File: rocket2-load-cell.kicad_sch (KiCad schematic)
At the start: 42 parts, among them J1 SWD, J2 629105150521, J3 PJ-002A, J4 Conn_01x02, U1 STM32F103C8Tx, U3 LD1117V33, Y1 16MHz

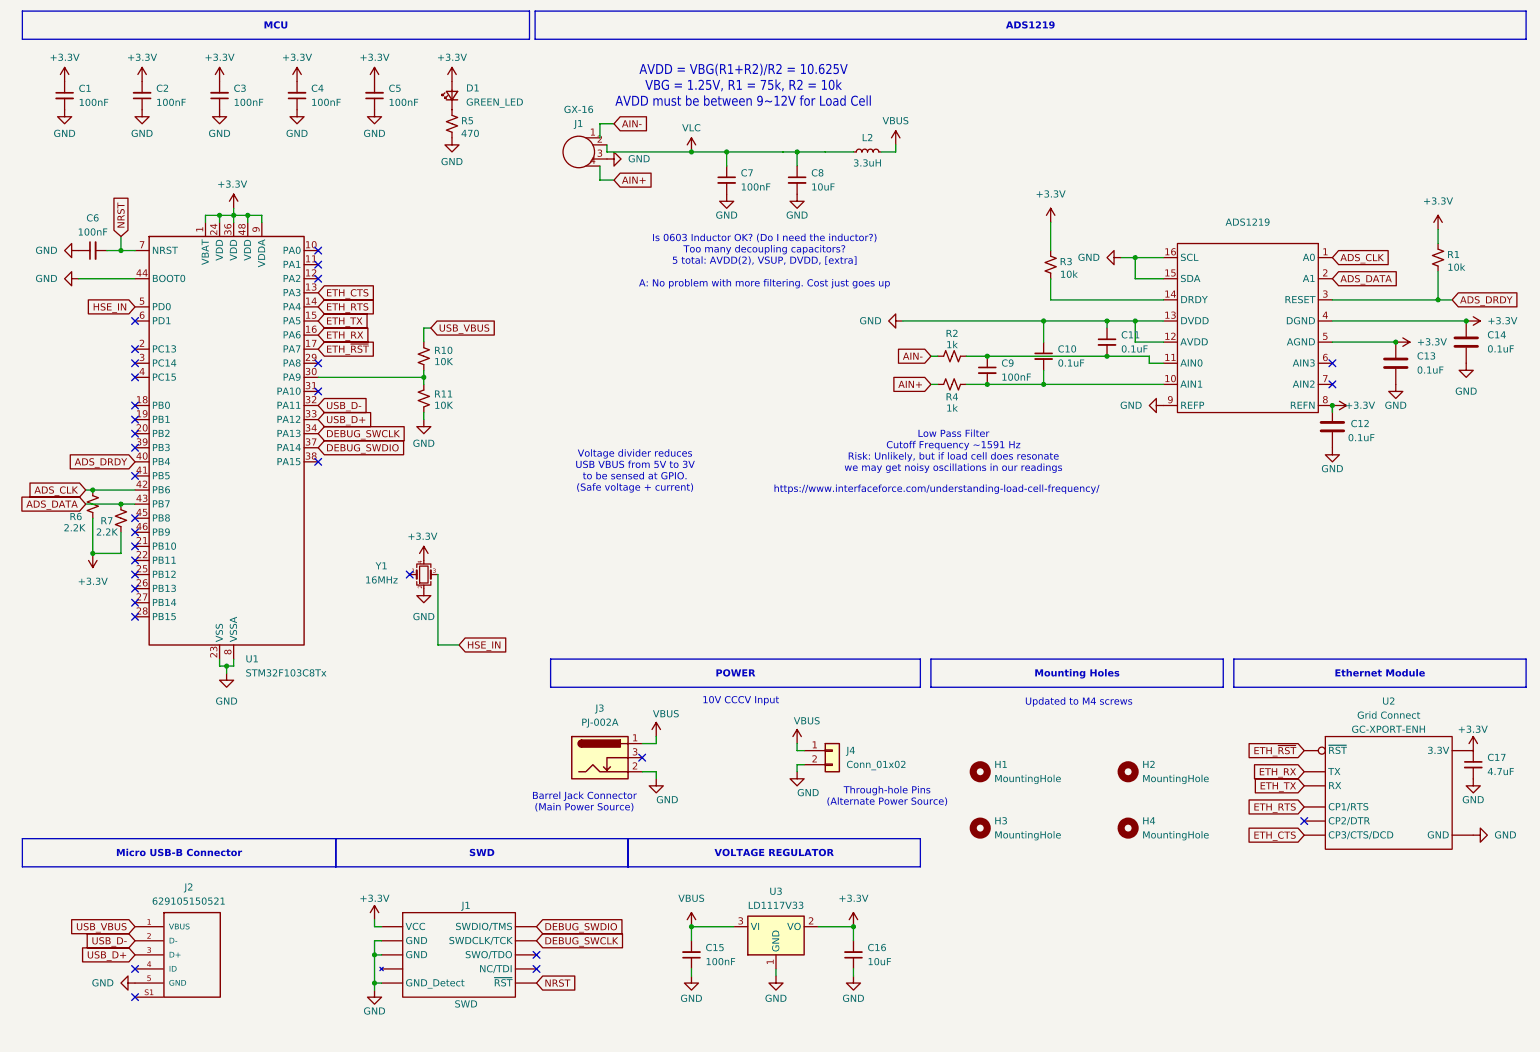
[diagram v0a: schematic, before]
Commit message: Layout adjustments
Layout revisions based on CDR feedback
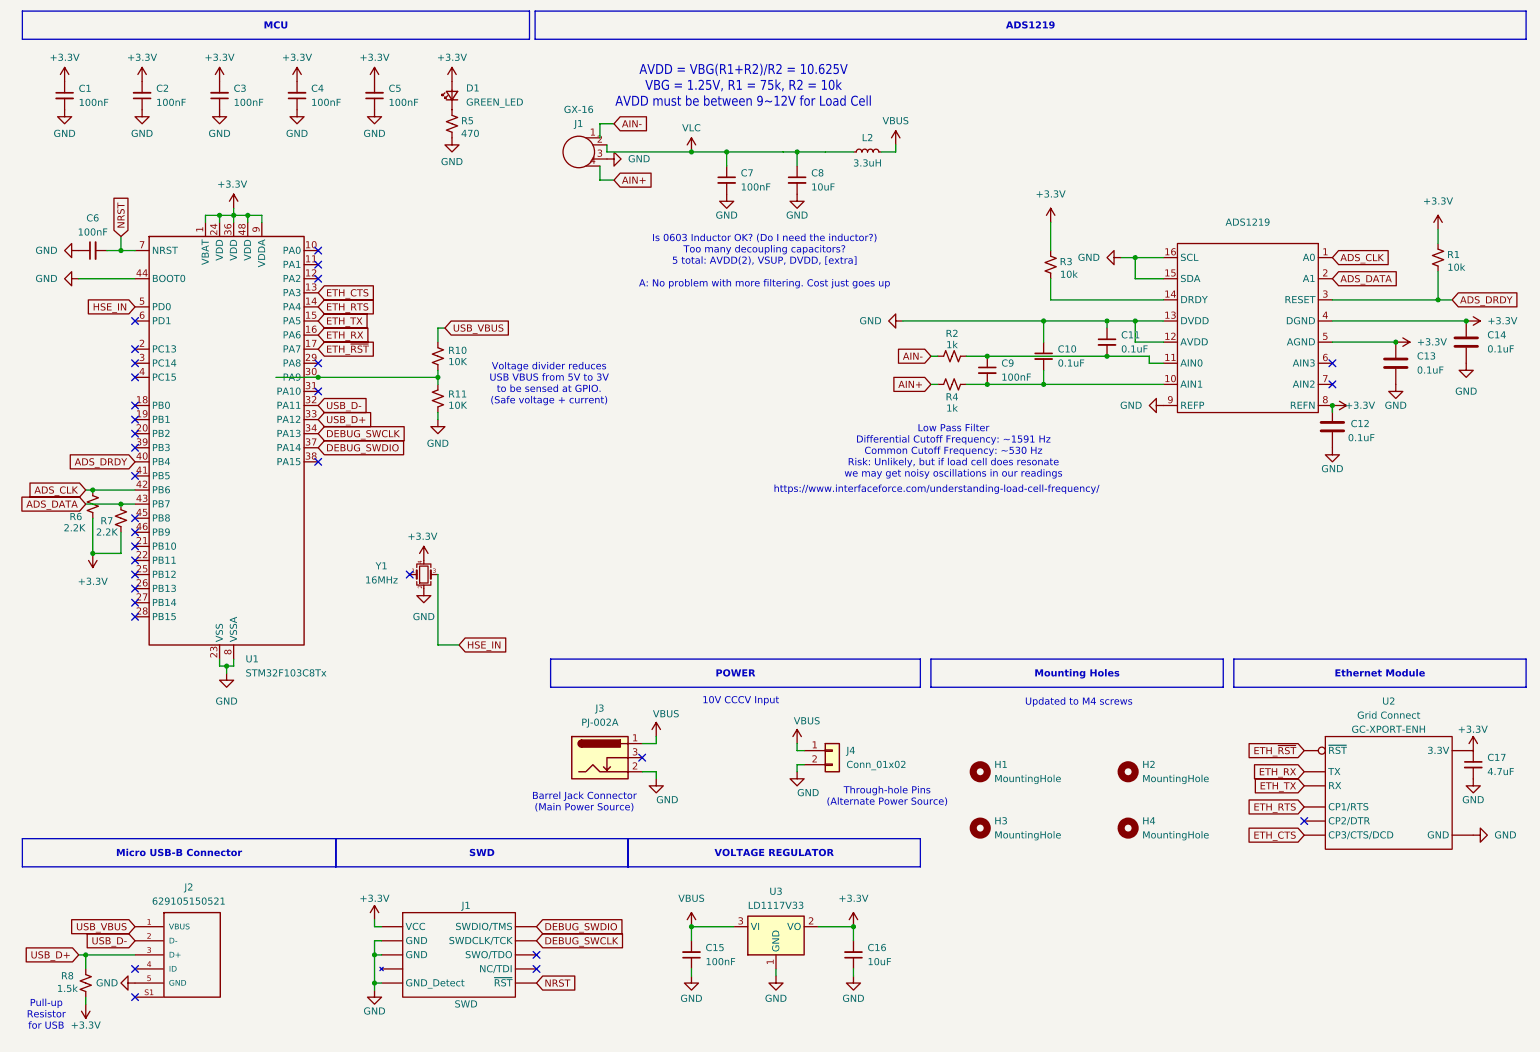
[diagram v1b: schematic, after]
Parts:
- added R8: 1.5k, Resistor_SMD:R_0603_1608Metric, symbol Device:R_Small_US
- U3: footprint Package_TO_SOT_THT:TO-220-3_Vertical -> Package_TO_SOT_SMD:SOT-223-3_TabPin2
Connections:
- net +3.3V: now also R8.1
- net USB_D+: now also R8.2
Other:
- note added: "Low Pass Filter Differential Cutoff Frequency: ~1591 Hz Common Cutoff Frequency: ~530 Hz Risk: Unlikely, but if load cell does resonate we may get noisy oscillations in our readings"
- note added: "Pull-up Resistor for USB"
- note removed: "Low Pass Filter Cutoff Frequency ~1591 Hz Risk: Unlikely, but if load cell does resonate we may get noisy oscillations in our readings"
- moved on the sheet: R10, R11

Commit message: Final Revisions pt. 2
Final PCB layout revisions (and a few schematic changes) from Robert (Added USB-C, removed excess vias, etc.)
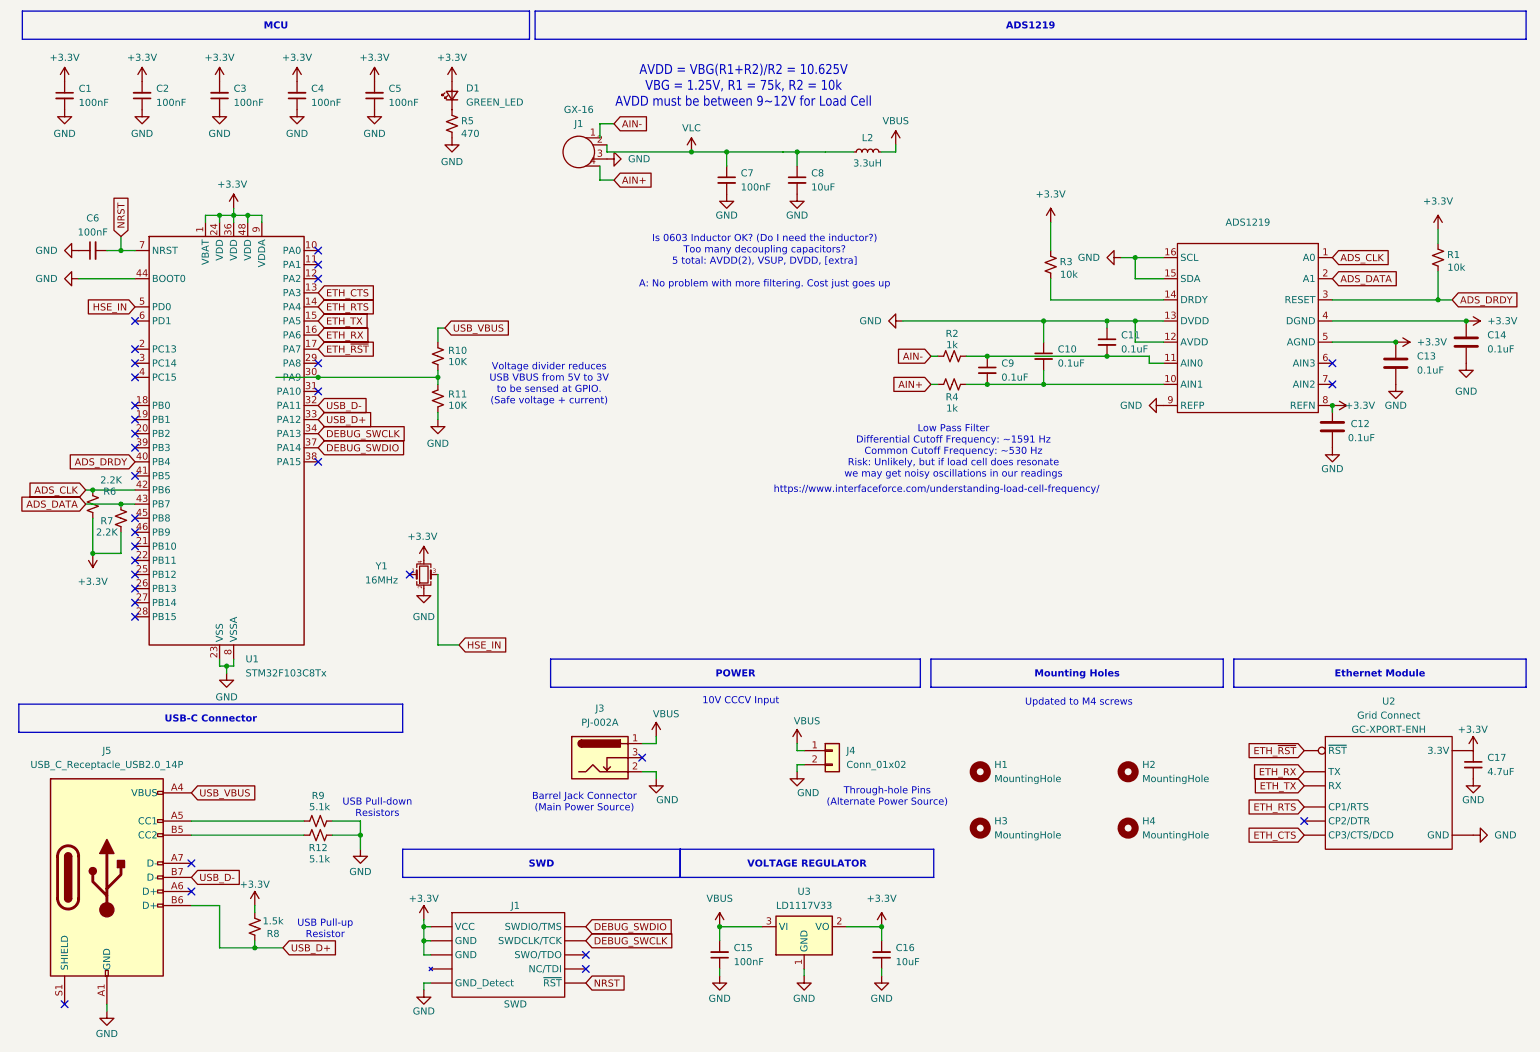
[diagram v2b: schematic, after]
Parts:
- removed J2: 629105150521, Connector_USB:USB_Micro-B_Wuerth_629105150521, symbol UCIRP-KiCAD-Lib:629105150521
- added J5: USB_C_Receptacle_USB2.0_14P, Connector_USB:USB_C_Receptacle_GCT_USB4110, symbol Connector:USB_C_Receptacle_USB2.0_14P
- added R12, R9: 5.1k, Resistor_SMD:R_0603_1608Metric, symbol Device:R_Small_US
- C9: value 100nF -> 0.1uF
- H1, H2, H3, H4: footprint MountingHole:MountingHole_4.3mm_M4 -> MountingHole:MountingHole_4.3mm_M4_ISO7380_Pad
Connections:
- net +3.3V: now also J1.3 (GND), J1.5 (GND), R6.2; no longer R6.1
- net ADS_CLK: now also R6.1; no longer R6.2
- net GND: now also J5.A1 (GND), J5.A12 (GND), J5.B1 (GND), J5.B12 (GND), R12.2, R9.2; no longer J1.3 (GND), J1.5 (GND)
- net USB_D+: now also J5.B6 (D+)
- net USB_D-: now also J5.B7 (D-)
- net USB_VBUS: now also J5.A4 (VBUS), J5.A9 (VBUS), J5.B4 (VBUS), J5.B9 (VBUS)
- new net: J5.A5 (CC1), R9.1
- new net: J5.B5 (CC2), R12.1
- no-connect marks 32 -> 33
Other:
- note added: "USB Pull-down Resistors"
- note added: "USB Pull-up Resistor"
- note removed: "Pull-up Resistor for USB"
- moved on the sheet: C15, C16, J1, R6, R8, U3

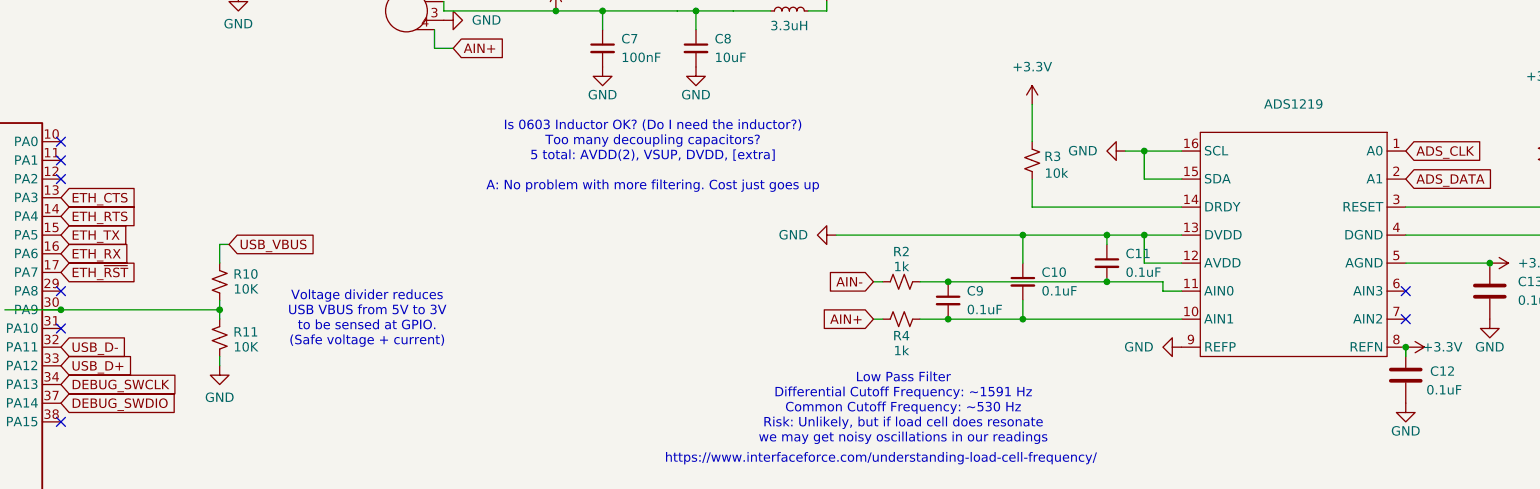
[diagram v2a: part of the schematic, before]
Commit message: Final Fix: ADC Layout
Corrected ADC Layout (Schematic was accidentally mirrored)
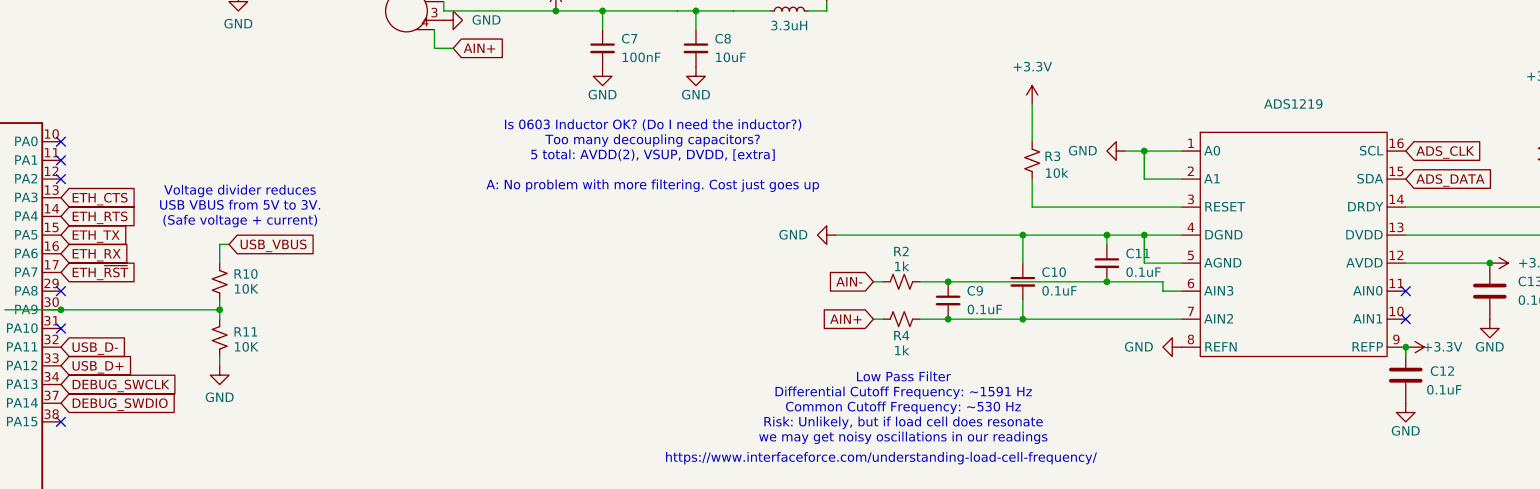
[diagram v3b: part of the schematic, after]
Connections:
- net +3.3V: now also ADS1219.12 (AVDD), ADS1219.13 (DVDD), ADS1219.9 (REFP); no longer ADS1219.4 (DGND), ADS1219.5 (AGND), ADS1219.8 (REFN)
- net ADS_CLK: now also ADS1219.16 (SCL); no longer ADS1219.1 (A0)
- net ADS_DATA: now also ADS1219.15 (SDA); no longer ADS1219.2 (A1)
- net ADS_DRDY: now also ADS1219.14 (DRDY); no longer ADS1219.3 (RESET)
- net GND: now also ADS1219.1 (A0), ADS1219.2 (A1), ADS1219.4 (DGND), ADS1219.5 (AGND), ADS1219.8 (REFN); no longer ADS1219.12 (AVDD), ADS1219.13 (DVDD), ADS1219.15 (SDA), ADS1219.16 (SCL), ADS1219.9 (REFP)
- net at C11.2, C9.1, R2.2: now also ADS1219.6 (AIN3); no longer ADS1219.11 (AIN0)
- net at C10.2, C9.2, R4.2: now also ADS1219.7 (AIN2); no longer ADS1219.10 (AIN1)
- net at R3.1: now also ADS1219.3 (RESET); no longer ADS1219.14 (DRDY)
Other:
- note added: "Voltage divider reduces USB VBUS from 5V to 3V. (Safe voltage + current)"
- note removed: "Voltage divider reduces USB VBUS from 5V to 3V to be sensed at GPIO. (Safe voltage + current)"
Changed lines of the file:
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@@
 	(generator_version "9.0")
 	(paper "A4")
-	(text "Voltage divider reduces \nUSB VBUS from 5V to 3V \nto be sensed at GPIO.\n(Safe voltage + current)\n"
+	(text "Voltage divider reduces \nUSB VBUS from 5V to 3V. \n(Safe voltage + current)\n"
 		(exclude_from_sim no)
-		(at 107.696 80.01 0)
+		(at 90.424 64.77 0)
 		(effects
 			(font
@@
 		(lib_id "load-cell-lib:ADS1219")
 		(at 233.68 69.85 0)
-		(mirror y)
 		(unit 1)
 		(exclude_from_sim no)

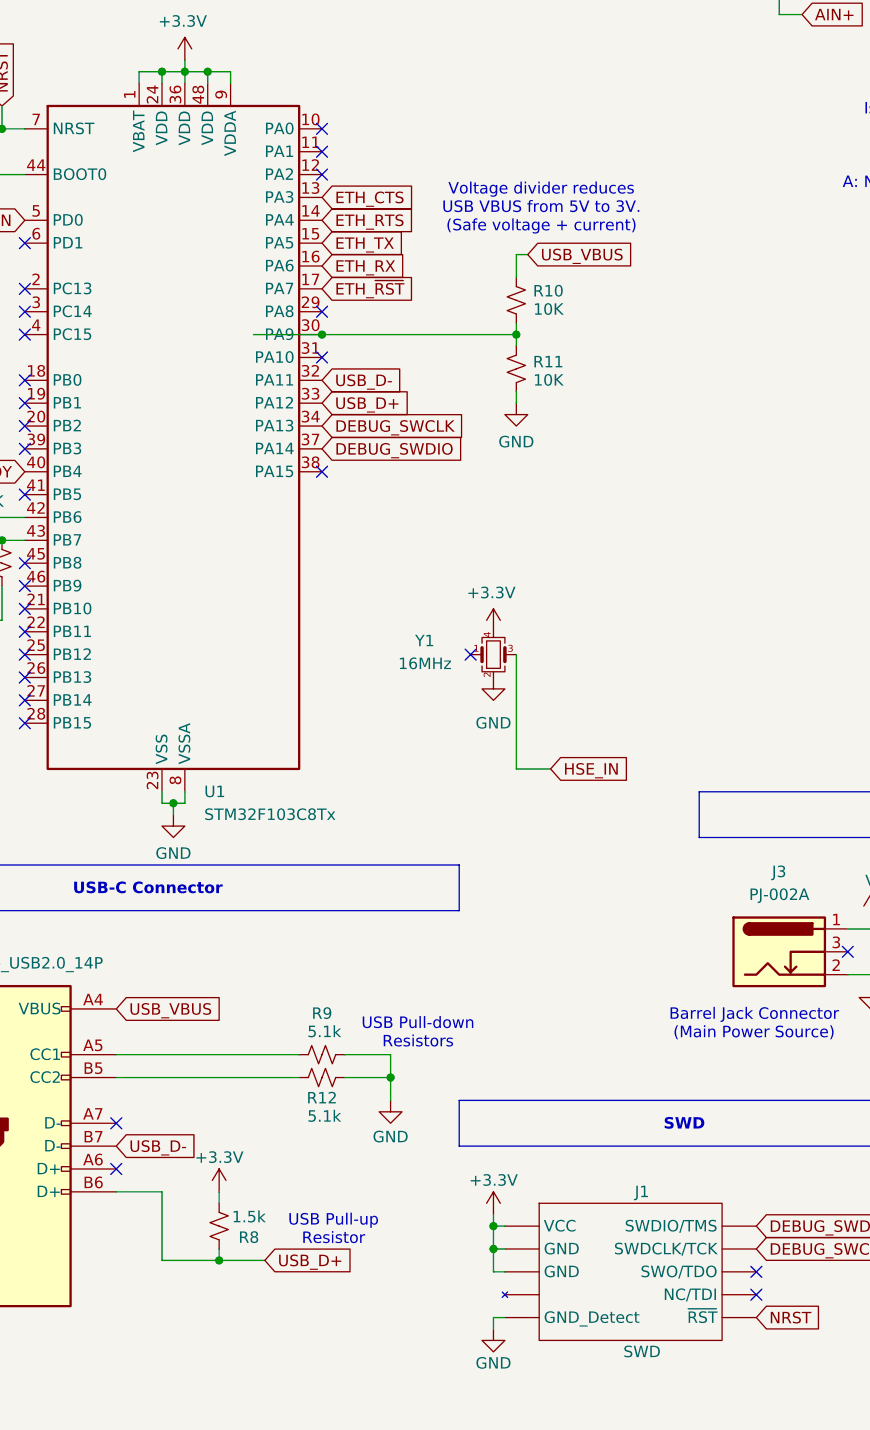
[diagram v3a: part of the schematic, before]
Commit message: LC v1.5 Fixes (Pt. 1)
Fixes shorts, pin configurations, among other vital details
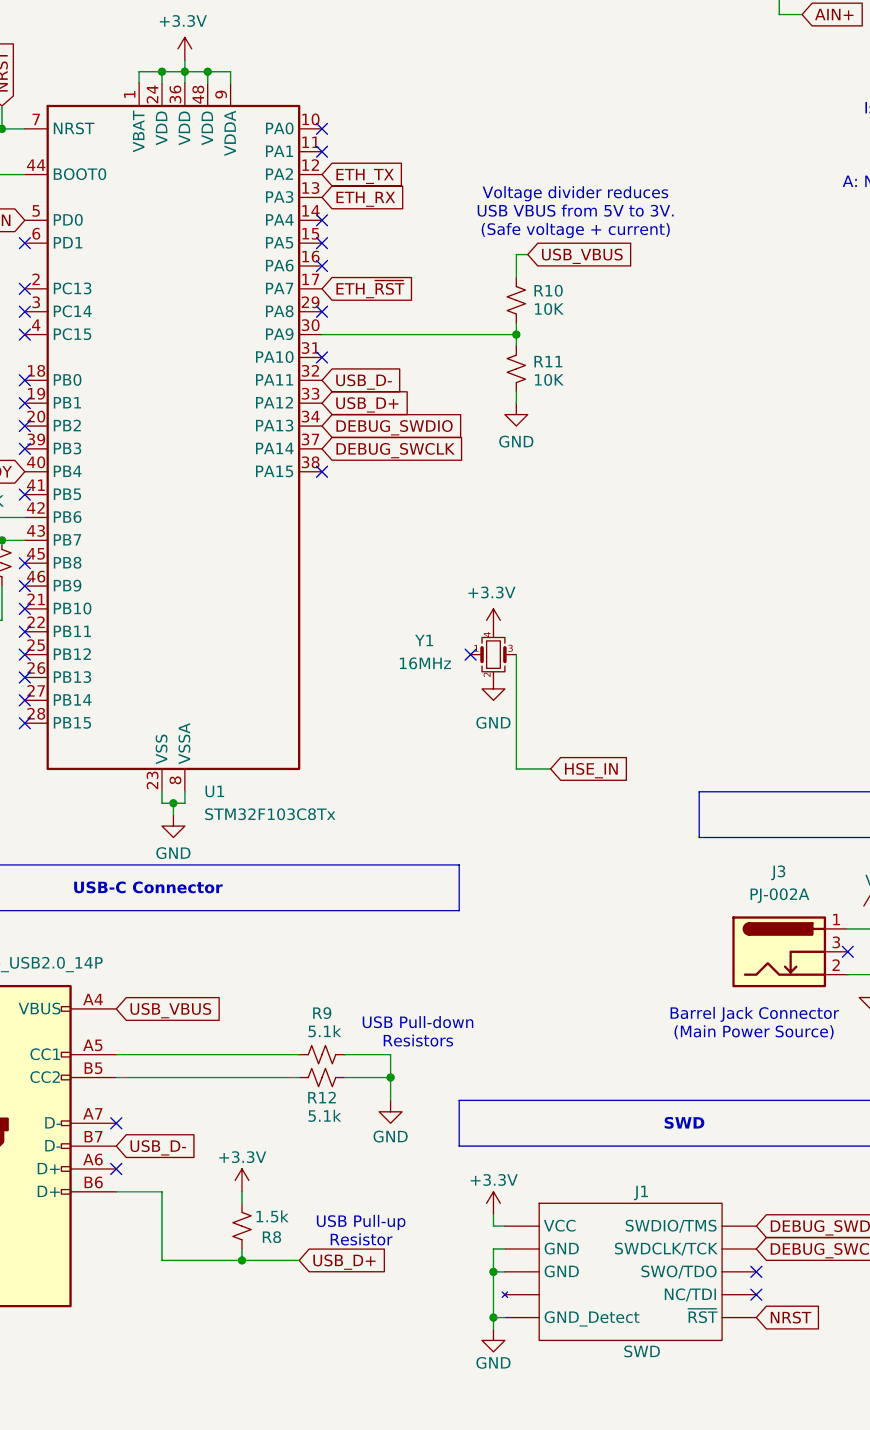
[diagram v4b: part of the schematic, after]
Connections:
- net +3.3V: no longer J1.3 (GND), J1.5 (GND)
- net DEBUG_SWCLK: now also U1.37 (PA14); no longer U1.34 (PA13)
- net DEBUG_SWDIO: now also U1.34 (PA13); no longer U1.37 (PA14)
- net ETH_CTS: no longer U1.13 (PA3)
- net ETH_RTS: no longer U1.14 (PA4)
- net ETH_RX: now also U1.13 (PA3); no longer U1.16 (PA6)
- net ETH_TX: now also U1.12 (PA2); no longer U1.15 (PA5)
- net GND: now also J1.3 (GND), J1.5 (GND)
- no-connect marks 33 -> 35
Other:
- moved on the sheet: R8
